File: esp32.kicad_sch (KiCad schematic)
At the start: 48 parts, among them J4 TC2030-IDC, J5 Conn_01x04, J6 Conn_01x06, J8 USB_C_Receptacle_USB2.0, SW1 SWITCH-SPST, SW2 SWITCH-SPST, U5 SN74AVC4T774, U6 ESP32-S3-WROOM-1, Y1 32.768kHz

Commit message: sch update done
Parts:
- removed TP12, TP13: TestPoint, TestPoint:TestPoint_Pad_D1.0mm, symbol Connector:TestPoint
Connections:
- net ALERT_TEMP: now reaches U6.4 (GPIO4/TOUCH4/ADC1_CH3)
- net OVERT_TEMP: now reaches U6.5 (GPIO5/TOUCH5/ADC1_CH4)
- net 1V8_IO renamed 1V2_IO
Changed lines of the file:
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@@
 		)
 	)
-	(label "1V8"
+	(label "1V2"
 		(at 60.96 157.48 0)
 		(fields_autoplaced yes)
@@
 		)
 	)
-	(hierarchical_label "1V8_IO"
+	(hierarchical_label "1V2_IO"
 		(shape input)
 		(at 24.13 157.48 180)
@@
 		(shape input)
 		(at 21.59 125.73 180)
+		(fields_autoplaced yes)
+		(effects
+			(font
+				(size 1.27 1.27)
+			)
+			(justify right)
+		)
+	)
+	(hierarchical_label "OVERT_TEMP"
+		(shape bidirectional)
+		(at 62.23 88.9 180)
+		(fields_autoplaced yes)
+		(effects
+			(font
+				(size 1.27 1.27)
+			)
+			(justify right)
+		)
+	)
+	(hierarchical_label "ALERT_TEMP"
+		(shape bidirectional)
+		(at 62.23 86.36 180)
 		(fields_autoplaced yes)
 		(effects
@@
 	(symbol
 		(lib_id "Connector:TestPoint")
-		(at 62.23 86.36 90)
-		(unit 1)
-		(exclude_from_sim no)
-		(in_bom no)
-		(on_board yes)
-		(dnp no)
-		(property "Reference" "TP12"
-			(at 55.88 86.36 90)
-			(effects
-				(font
-					(size 1.27 1.27)
-				)
-			)
-		)
-		(property "Value" "TestPoint"
-			(at 56.515 85.0901 90)
-			(effects
-				(font
-					(size 1.27 1.27)
-				)
-				(justify left)
-				(hide yes)
-			)
-		)
-		(property "Footprint" "TestPoint:TestPoint_Pad_D1.0mm"
-			(at 62.23 81.28 0)
-			(effects
-				(font
-					(size 1.27 1.27)
-				)
-				(hide yes)
-			)
-		)
-		(property "Datasheet" "~"
-			(at 62.23 81.28 0)
-			(effects
-				(font
-					(size 1.27 1.27)
-				)
-				(hide yes)
-			)
-		)
-		(property "Description" ""
-			(at 62.23 86.36 0)
-			(effects
-				(font
-					(size 1.27 1.27)
-				)
-				(hide yes)
-			)
-		)
-		(pin "1"
-		)
-		(instances
-			(project "bitaxeHex"
-				(path "/e63e39d7-6ac0-4ffd-8aa3-1841a4541b55/ca857324-2ec8-447e-bd58-90d0c2e6b6d7"
-					(reference "TP12")
-					(unit 1)
-				)
-			)
-		)
-	)
-	(symbol
-		(lib_id "Connector:TestPoint")
 		(at 194.31 109.22 270)
 		(mirror x)
@@
 					(unit 1)
 				)
-			)
-		)
-	)
-	(symbol
-		(lib_id "Connector:TestPoint")
-		(at 62.23 88.9 90)
-		(unit 1)
-		(exclude_from_sim no)
-		(in_bom no)
-		(on_board yes)
-		(dnp no)
-		(property "Reference" "TP13"
-			(at 55.88 88.9 90)
-			(effects
-				(font
-					(size 1.27 1.27)
-				)
-			)
-		)
-		(property "Value" "TestPoint"
-			(at 56.515 87.6301 90)
-			(effects
-				(font
-					(size 1.27 1.27)
-				)
-				(justify left)
-				(hide yes)
-			)
-		)
-		(property "Footprint" "TestPoint:TestPoint_Pad_D1.0mm"
-			(at 62.23 83.82 0)
-			(effects
-				(font
-					(size 1.27 1.27)
-				)
-				(hide yes)
-			)
-		)
-		(property "Datasheet" "~"
-			(at 62.23 83.82 0)
-			(effects
-				(font
-					(size 1.27 1.27)
-				)
-				(hide yes)
-			)
-		)
-		(property "Description" ""
-			(at 62.23 88.9 0)
-			(effects
-				(font
-					(size 1.27 1.27)
-				)
-				(hide yes)
-			)
-		)
-		(pin "1"
-		)
-		(instances
-			(project "bitaxeHex"
-				(path "/e63e39d7-6ac0-4ffd-8aa3-1841a4541b55/ca857324-2ec8-447e-bd58-90d0c2e6b6d7"
-					(reference "TP13")
-					(unit 1)
-				)

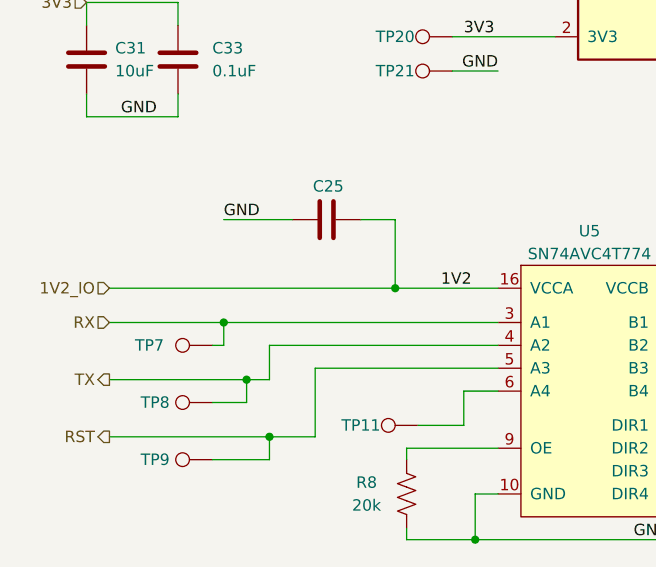
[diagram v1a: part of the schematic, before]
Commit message: Reset to 1V8
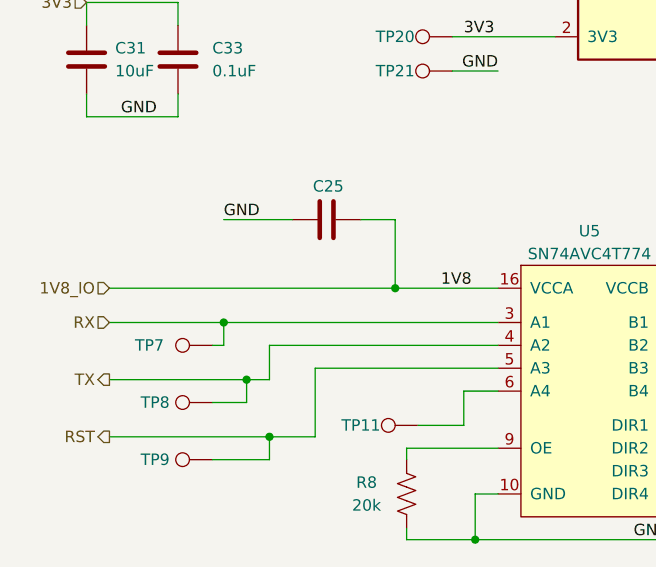
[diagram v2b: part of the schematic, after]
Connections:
- net 1V2_IO renamed 1V8_IO
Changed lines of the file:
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@@
 		)
 	)
-	(label "1V2"
+	(label "1V8"
 		(at 60.96 157.48 0)
 		(fields_autoplaced yes)
@@
 		)
 	)
-	(hierarchical_label "1V2_IO"
+	(hierarchical_label "1V8_IO"
 		(shape input)
 		(at 24.13 157.48 180)
